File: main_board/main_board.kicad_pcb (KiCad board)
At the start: 4 copper layers, 85 x 55 mm, 53 parts, among them J1 USB_B_Micro, J2 Conn_ARM_JTAG_SWD_10, Q1 NX3008PBK,215, Q2 T2N7002AK,LM, U1 SSD1306, U2 ESP32-S2-SOLO, U3 TLV62568PDRLT, U4 MCP73832, Y1 SC32S-7PF20PPM

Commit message: Add logo
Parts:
- added G1: ~, main_board_parts:logo, B.Cu at (90.3, 70.6)
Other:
- board text added: "v1r2 Not for medical use"
- board text removed: "Card/IO v1r2 Not for medical use"
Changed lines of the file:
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@@
     )
+  )
+  (footprint "main_board_parts:logo" (layer "B.Cu")
+    (at 90.35 70.6 180)
+    (property "Sheetfile" "main_board.kicad_sch")
+    (property "Sheetname" "")
+    (attr smd)
+    (fp_text reference "G1" (at 0 -9.8 unlocked) (layer "B.SilkS") hide
+        (effects (font (size 1 1) (thickness 0.15)) (justify mirror))
+    )
+    (fp_text value "~" (at 0 -11.3 unlocked) (layer "B.Fab") hide
+        (effects (font (size 1 1) (thickness 0.15)) (justify mirror))
+    )
+    (fp_text user "Card IO" (at -12 -2.2 unlocked) (layer "B.SilkS")
+        (effects (font (size 3 3) (thickness 0.5) bold) (justify left bottom mirror))
+    )
+    (fp_text user "${REFERENCE}" (at 0 -12.8 unlocked) (layer "B.Fab") hide
+        (effects (font (size 1 1) (thickness 0.15)) (justify mirror))
+    )
+    (fp_line (start -11.8 -3) (end -1.8 -3)
+      (stroke (width 0.5) (type default)) (layer "B.SilkS"))
+    (fp_line (start -1.8 -3) (end -0.6 1.8)
+      (stroke (width 0.5) (type default)) (layer "B.SilkS"))
+    (fp_line (start -0.6 1.8) (end 0.4 -6.8)
+      (stroke (width 0.5) (type default)) (layer "B.SilkS"))
+    (fp_line (start 0.4 -6.8) (end 1.4 -3)
+      (stroke (width 0.5) (type default)) (layer "B.SilkS"))
+    (fp_line (start 1.4 -3) (end 5 -3)
+      (stroke (width 0.5) (type default)) (layer "B.SilkS"))
   )
   (footprint "main_board_parts:Electrode" locked (layer "B.Cu")
@@
     (effects (font (size 1 1) (thickness 0.2) bold) (justify left bottom mirror))
   )
-  (gr_text "Card/IO v1r2\nNot for medical use" (at 129.9 53.15) (layer "B.SilkS")
+  (gr_text "v1r2 Not for\nmedical use" (at 101.85 77.3) (layer "B.SilkS")
     (effects (font (size 1 1) (thickness 0.15)) (justify left bottom mirror))
   )

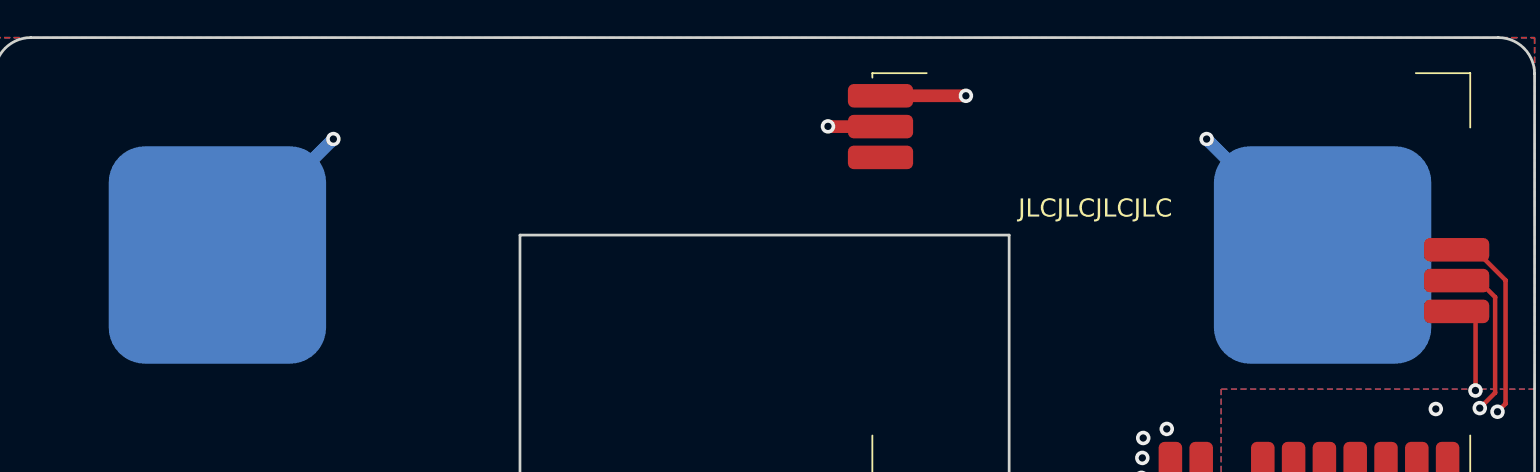
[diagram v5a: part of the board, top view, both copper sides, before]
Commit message: Fix #21: Add split electrodes
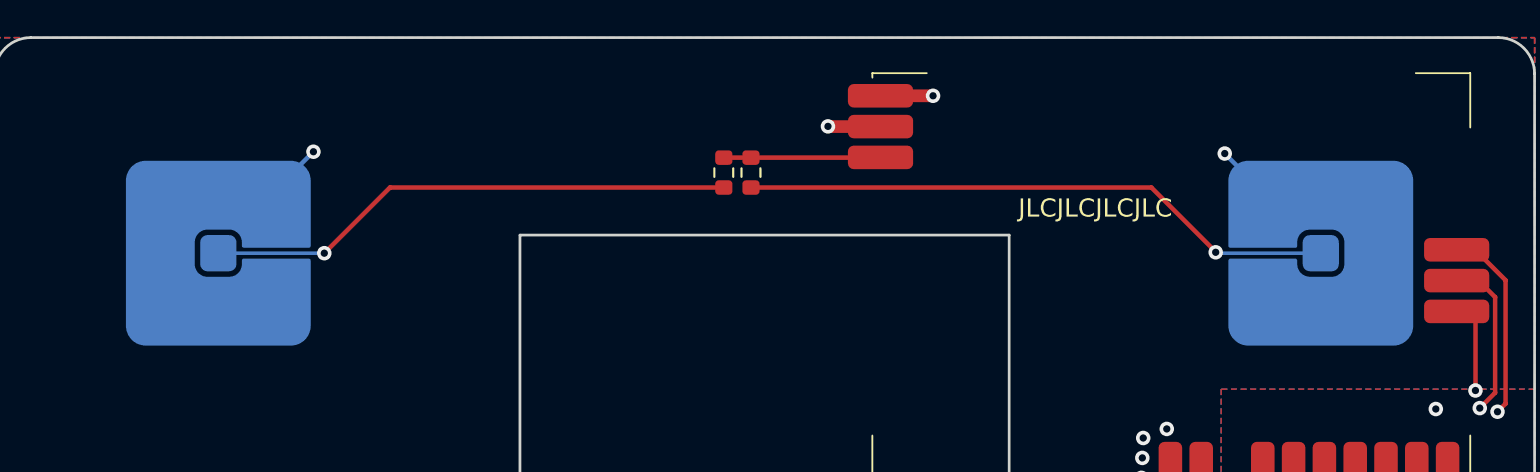
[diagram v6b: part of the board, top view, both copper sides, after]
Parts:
- removed EL1, ER1: ~, main_board_parts:Electrode
- added E1: ~, main_board_parts:SplitElectrode, B.Cu at (153.2, 56.9)
- added E2: ~, main_board_parts:SplitElectrode, B.Cu at (92.3, 56.9)
- added R16: 1M, Resistor_SMD:R_0603_1608Metric, F.Cu at (121.8, 52.5)
- added R17: 1M, Resistor_SMD:R_0603_1608Metric, F.Cu at (120.2, 52.5)
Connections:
- M1 pad 3: unconnected-(M1-RLD_OUT-Pad3) -> Net-(M1-RLD_OUT)
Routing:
- net Net-(E1-Pad1): track 0.00 -> 33.0 mm, vias 0 -> 1
- net Net-(E2-Pad1): track 0.00 -> 29.4 mm, vias 0 -> 1
- net Net-(M1-ECG_R): track 37.2 -> 48.8 mm
- net Net-(M1-RLD_OUT): track 0.00 -> 8.66 mm
- net Net-(M1-ECG_L): track 28.9 -> 26.6 mm
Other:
- board text added: "Not for medical use"
- board text added: "v1r2"
- board text removed: "v1r2 Not for medical use"

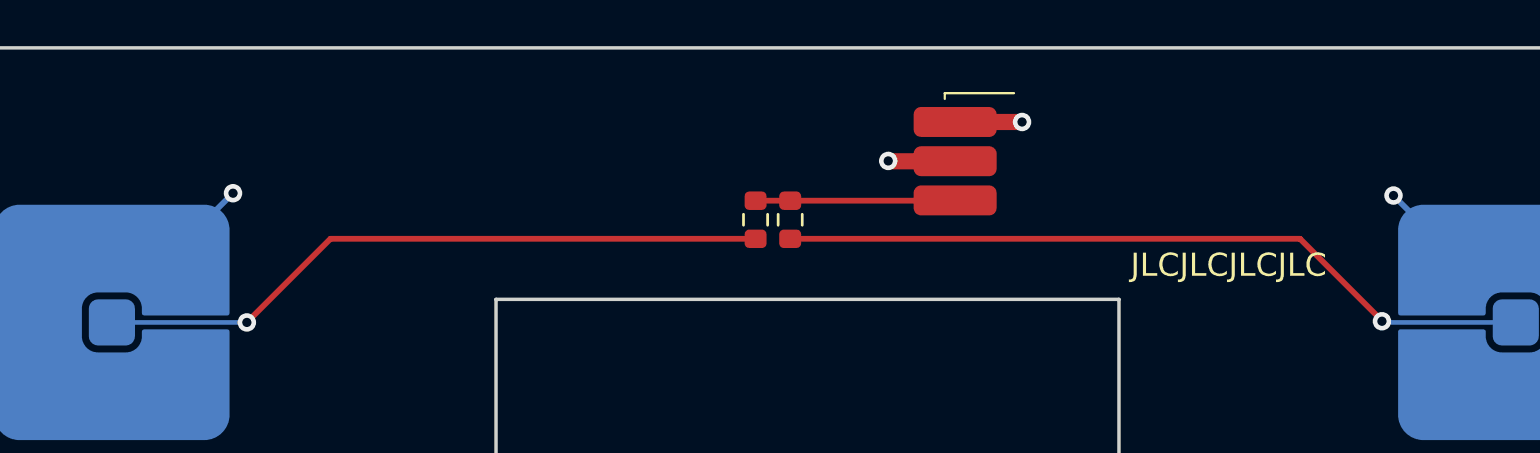
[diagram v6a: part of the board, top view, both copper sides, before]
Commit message: Fix #3: add QR code, exclude some parts from BOM
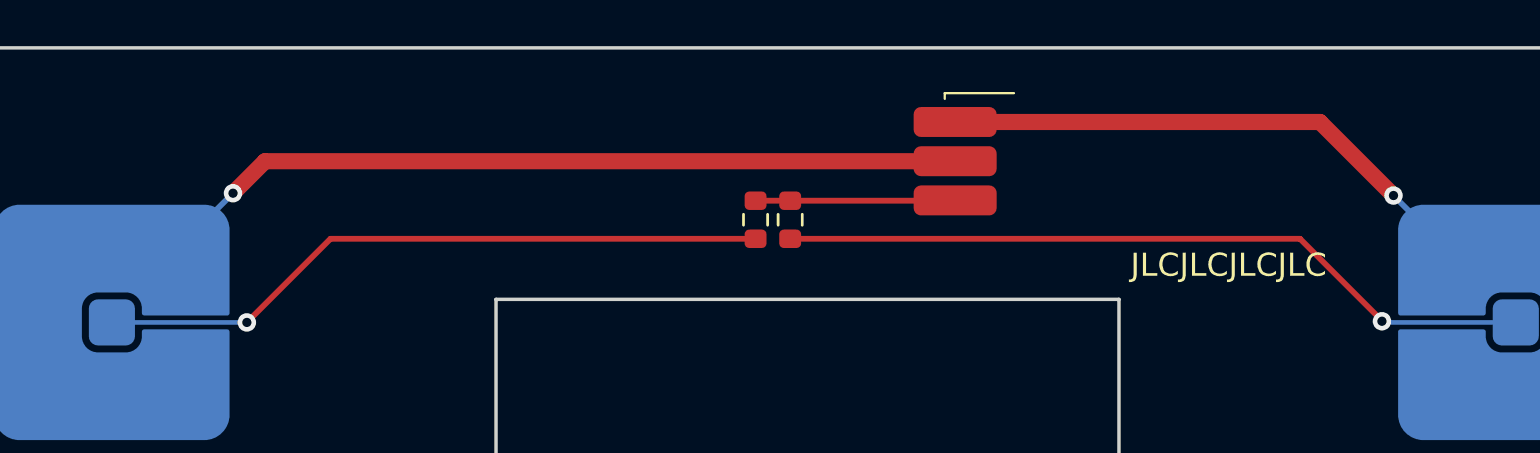
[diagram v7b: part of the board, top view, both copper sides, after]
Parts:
- added QR1: SYM_Magnet_Large, main_board_parts:website-qr, B.Cu at (92.8, 75.0)
- moved G1 38.3 mm to (121.3, 48.1)
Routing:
- net Net-(M1-ECG_R): track 48.8 -> 47.4 mm, vias 2 -> 1
- net Net-(M1-ECG_L): vias 2 -> 1

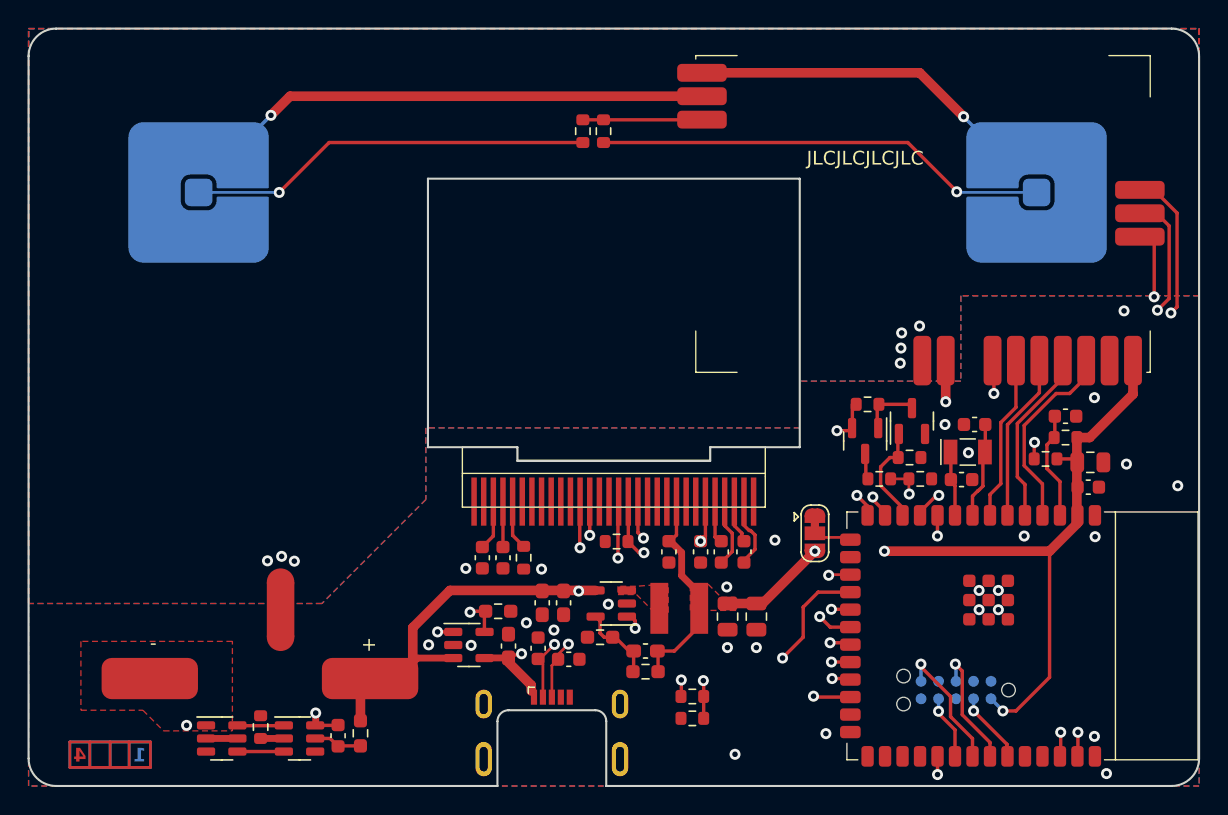
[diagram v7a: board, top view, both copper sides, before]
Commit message: Close #25: Add MAX17055
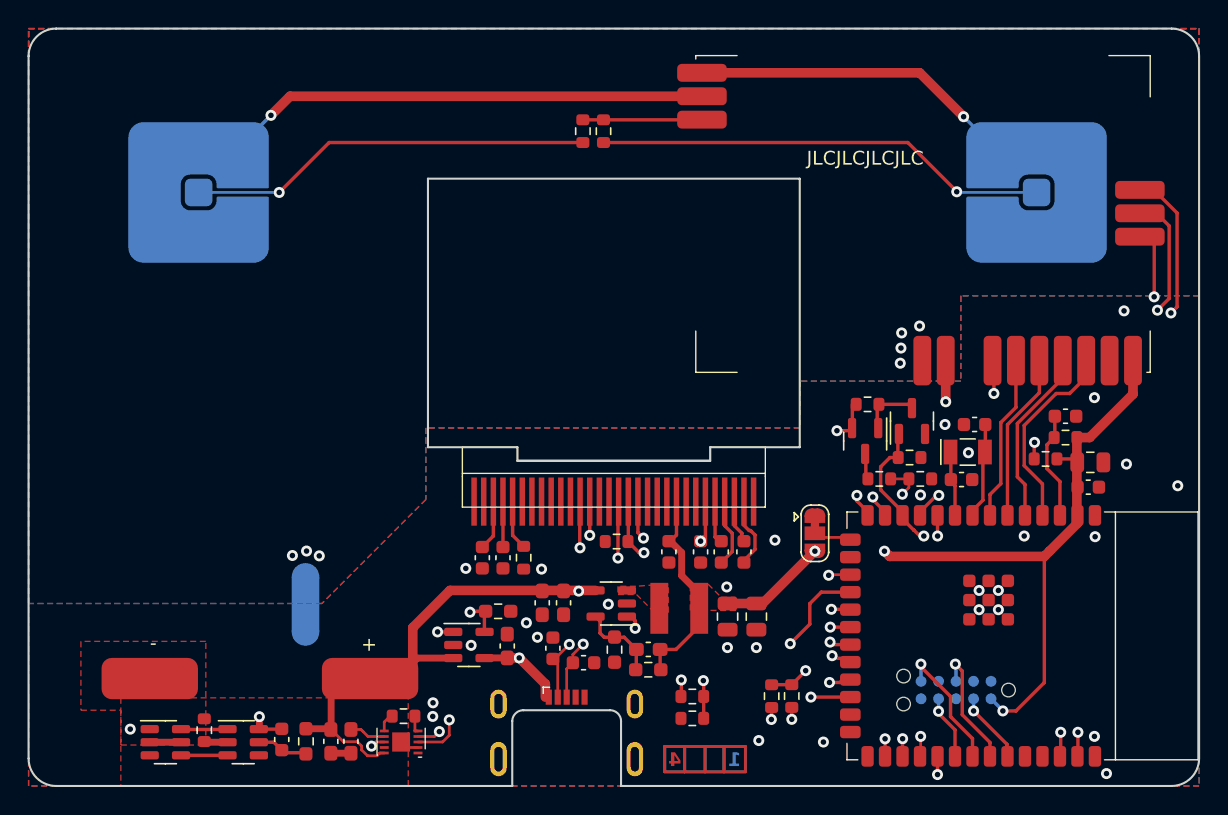
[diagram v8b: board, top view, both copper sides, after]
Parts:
- added C21: 100nF, Capacitor_SMD:C_0603_1608Metric_Pad1.08x0.95mm_HandSolder, F.Cu at (102.0, 96.8)
- added C22: 470nF, Capacitor_SMD:C_0603_1608Metric_Pad1.08x0.95mm_HandSolder, F.Cu at (103.4, 96.8)
- added R18: 0.01R, Resistor_SMD:R_0603_1608Metric, F.Cu at (107.2, 94.9)
- added R19: 4k7, Resistor_SMD:R_0603_1608Metric, F.Cu at (135.4, 93.5)
- added R20: 4k7, Resistor_SMD:R_0603_1608Metric, F.Cu at (134.0, 93.5)
- added U7: MAX17055, main_board_parts:MAX17055, F.Cu at (107.1, 96.8)
- NT1: moved to B.Cu
- moved U5 4.10 mm to (95.6, 96.8)
- moved U6 4.10 mm to (89.9, 96.8)
- moved C14 4.10 mm to (98.4, 96.6)
- moved R15 4.10 mm to (92.8, 95.9)
- moved R6 4.00 mm to (100.1, 96.8)
- moved NT1 1.85 mm to (100.1, 86.8)
- moved R8 1.38 mm to (122.5, 90.1), turned to -90 degrees
- moved C11 1.10 mm to (120.3, 91.0)
- moved C10 1.08 mm to (118.1, 90.0)
- moved J1 1.08 mm to (119.1, 93.0)
- moved R7 0.24 mm to (125.0, 91.6)
- moved C17 0.23 mm to (125.0, 90.1)
- moved C19 0.09 mm to (114.8, 89.8)
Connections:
- R15 pad 2: GND -> Earth
- U2 pad 28: unconnected-(U2-IO35-Pad28) -> /BATT_SDA
- U2 pad 29: unconnected-(U2-IO36-Pad29) -> /BATT_SCL
- U2 pad 30: unconnected-(U2-IO37-Pad30) -> /BATT_ALERT
- U6 pad 3: GND -> Earth
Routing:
- net /BATT_ALERT: track 0.00 -> 46.6 mm, vias 0 -> 2
- net /BATT_SCL: track 0.00 -> 42.6 mm, vias 0 -> 3
- net /BATT_SDA: track 0.00 -> 40.4 mm, vias 0 -> 3
- net /ADC_EN: track 7.46 -> 28.1 mm, vias 0 -> 2
- net +BATT: track 81.1 -> 92.1 mm
- net Earth: track 0.00 -> 4.23 mm
- net Net-(U7-REG): track 0.00 -> 2.63 mm
- net GND: track 0.00 -> 1.35 mm, vias 27 -> 29
- net /USB_D-: track 34.4 -> 33.1 mm
- net /USB_D+: track 31.6 -> 30.5 mm
- added copper zone on F.Cu, net Earth
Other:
- outline, holes or cut-outs redrawn
